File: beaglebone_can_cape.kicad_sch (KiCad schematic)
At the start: 26 parts, among them J1 Conn_01x02_Pin, J2 Conn_01x02_Pin, J3 DTM15-12PA, J4 Conn_02x02_Top_Bottom, J5 Battery Harness, P8 BeagleBone_Black_Header, P9 BeagleBone_Black_Header, U1 TCAN332, U2 TCAN332, U3 LMR51430

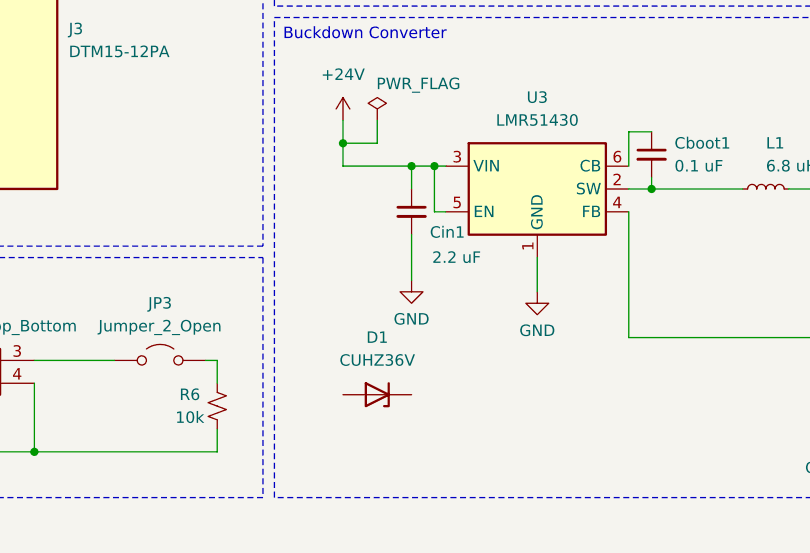
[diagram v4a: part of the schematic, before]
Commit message: added tvs diode to schem
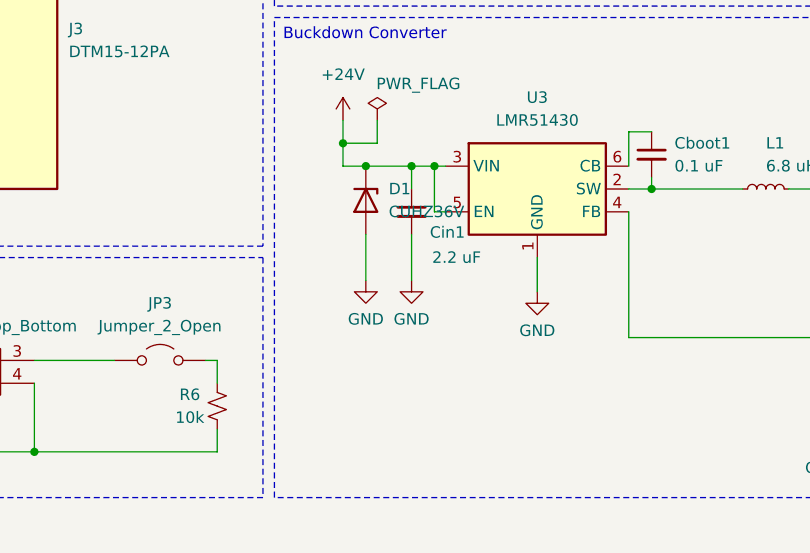
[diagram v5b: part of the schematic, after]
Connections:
- net +24V: now also D1.1 (K)
- net GND: now also D1.2 (A)
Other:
- moved on the sheet: D1
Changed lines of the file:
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@@
 	)
 	(junction
+		(at 96.52 139.7)
+		(diameter 0)
+		(color 0 0 0 0)
+	)
+	(junction
 		(at 104.14 139.7)
 		(diameter 0)
@@
 	(wire
 		(pts
+			(xy 96.52 147.32) (xy 96.52 152.4)
+		)
+		(stroke
+			(width 0)
+			(type default)
+		)
+	)
+	(wire
+		(pts
 			(xy 147.32 158.75) (xy 147.32 161.29)
 		)
@@
 	(wire
 		(pts
+			(xy 96.52 139.7) (xy 101.6 139.7)
+		)
+		(stroke
+			(width 0)
+			(type default)
+		)
+	)
+	(wire
+		(pts
 			(xy 138.43 46.99) (xy 140.97 46.99)
 		)
@@
 	(wire
 		(pts
-			(xy 93.98 139.7) (xy 101.6 139.7)
+			(xy 93.98 139.7) (xy 96.52 139.7)
 		)
 		(stroke
@@
 	(symbol
 		(lib_id "Diode:PTVS5V0Z1USK")
-		(at 97.79 165.1 180)
+		(at 96.52 143.51 270)
 		(unit 1)
 		(exclude_from_sim no)
@@
 		(fields_autoplaced yes)
 		(property "Reference" "D1"
-			(at 97.79 158.75 0)
+			(at 99.06 142.2399 90)
 			(effects
 				(font
 					(size 1.27 1.27)
 				)
+				(justify left)
 			)
 		)
 		(property "Value" "CUHZ36V"
-			(at 97.79 161.29 0)
+			(at 99.06 144.7799 90)
 			(effects
 				(font
 					(size 1.27 1.27)
 				)
+				(justify left)
 			)
 		)
 		(property "Footprint" "SeniorDesign:TVSDiode"
-			(at 97.79 160.655 0)
+			(at 92.075 143.51 0)
 			(effects
 				(font
@@
 		)
 		(property "Datasheet" "https://toshiba.semicon-storage.com/info/CUHZ36V_datasheet_en_20210917.pdf?did=70664&prodName=CUHZ36V"
-			(at 97.79 165.1 0)
+			(at 96.52 143.51 0)
 			(effects
 				(font
@@
 		)
 		(property "Description" ""
-			(at 97.79 165.1 0)
+			(at 96.52 143.51 0)
 			(effects
 				(font
@@
 					(unit 1)
 				)
+			)
+		)
+	)
+	(symbol
+		(lib_id "power:GND")
+		(at 96.52 152.4 0)
+		(unit 1)
+		(exclude_from_sim no)
+		(in_bom yes)
+		(on_board yes)
+		(dnp no)
+		(property "Reference" "#PWR022"
+			(at 96.52 158.75 0)
+			(effects
+				(font
+					(size 1.27 1.27)
+				)
+				(hide yes)
+			)
+		)
+		(property "Value" "GND"
+			(at 96.52 156.718 0)
+			(effects
+				(font
+					(size 1.27 1.27)
+				)
+			)
+		)
+		(property "Footprint" ""
+			(at 96.52 152.4 0)
+			(effects
+				(font
+					(size 1.27 1.27)
+				)
+				(hide yes)
+			)
+		)
+		(property "Datasheet" ""
+			(at 96.52 152.4 0)
+			(effects
+				(font
+					(size 1.27 1.27)
+				)
+				(hide yes)
+			)
+		)
+		(property "Description" "Power symbol creates a global label with name \"GND\" , ground"
+			(at 96.52 152.4 0)
+			(effects
+				(font
+					(size 1.27 1.27)
+				)
+				(hide yes)
+			)
+		)
+		(pin "1"
+		)
+		(instances
+			(project "beaglebone_can_cape"
+				(path "/e63e39d7-6ac0-4ffd-8aa3-1841a4541b55"
+					(reference "#PWR022")
+					(unit 1)
+				)

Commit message: pushing for nash work
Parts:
- J3: footprint Senior Design:TE_DTM15-12PA -> SeniorDesign:Deutsch_Marlin
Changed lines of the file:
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@@
 			)
 		)
-		(property "Footprint" "Senior Design:TE_DTM15-12PA"
+		(property "Footprint" "SeniorDesign:Deutsch_Marlin"
 			(at 57.15 127 0)
 			(effects

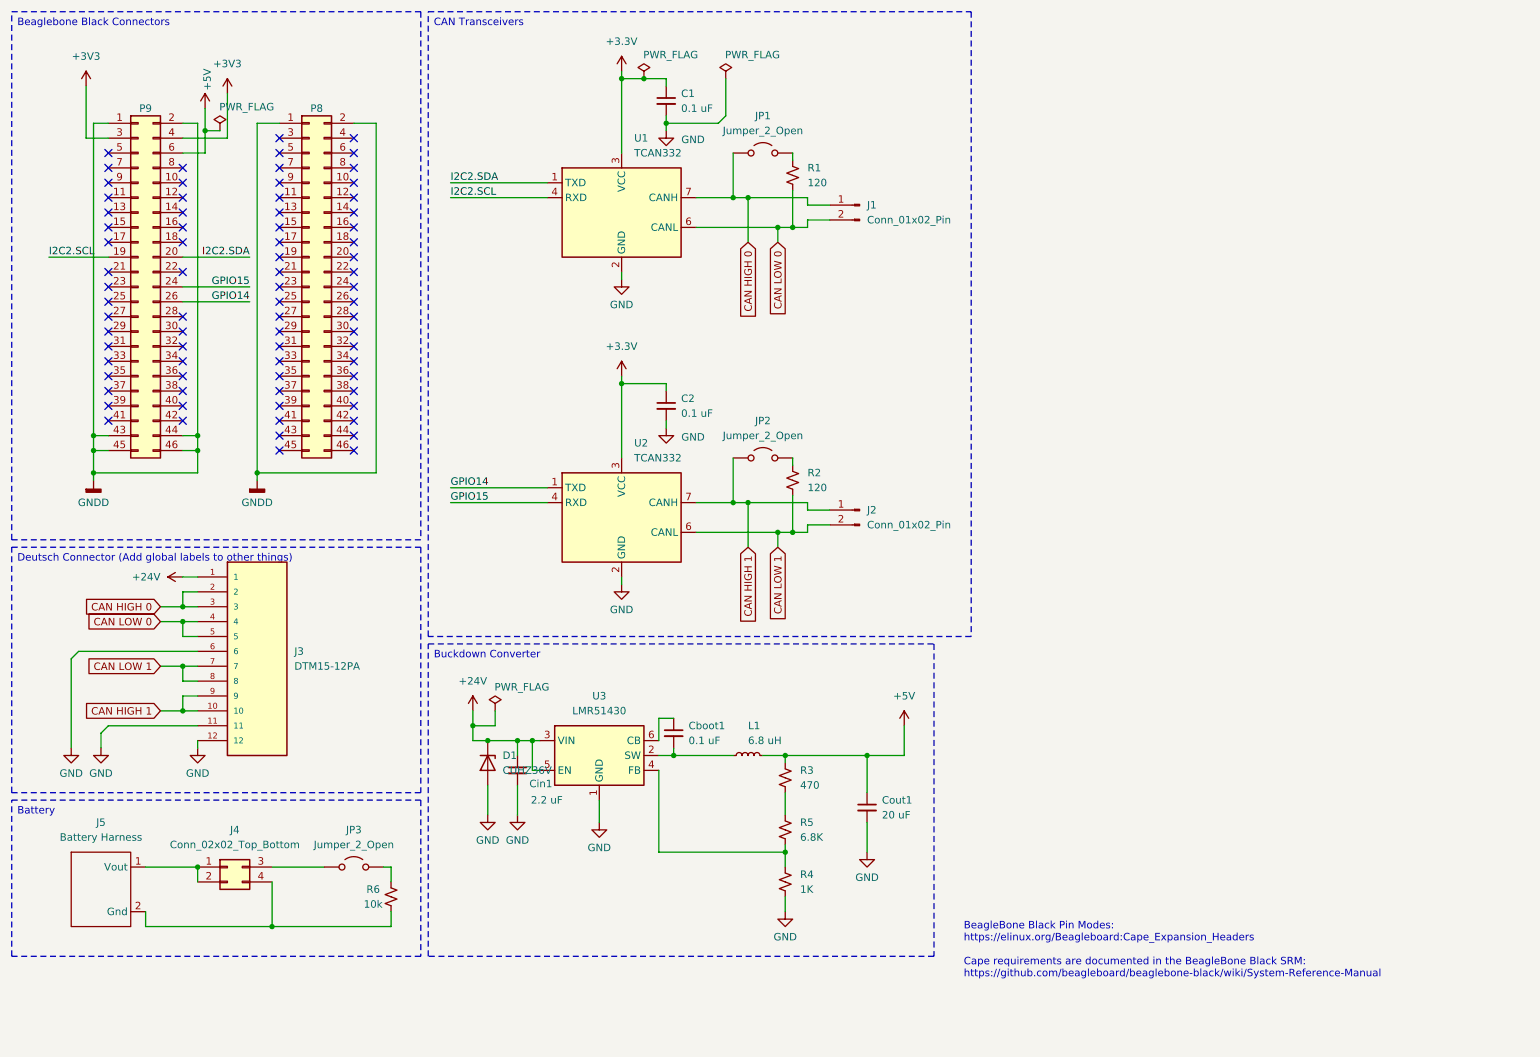
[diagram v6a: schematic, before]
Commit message: Implementing Deutsch + wiring
* Got rid of more errors and corrected more footprints. Going smoothly.
* Researched the TVS diode. cool stuff!
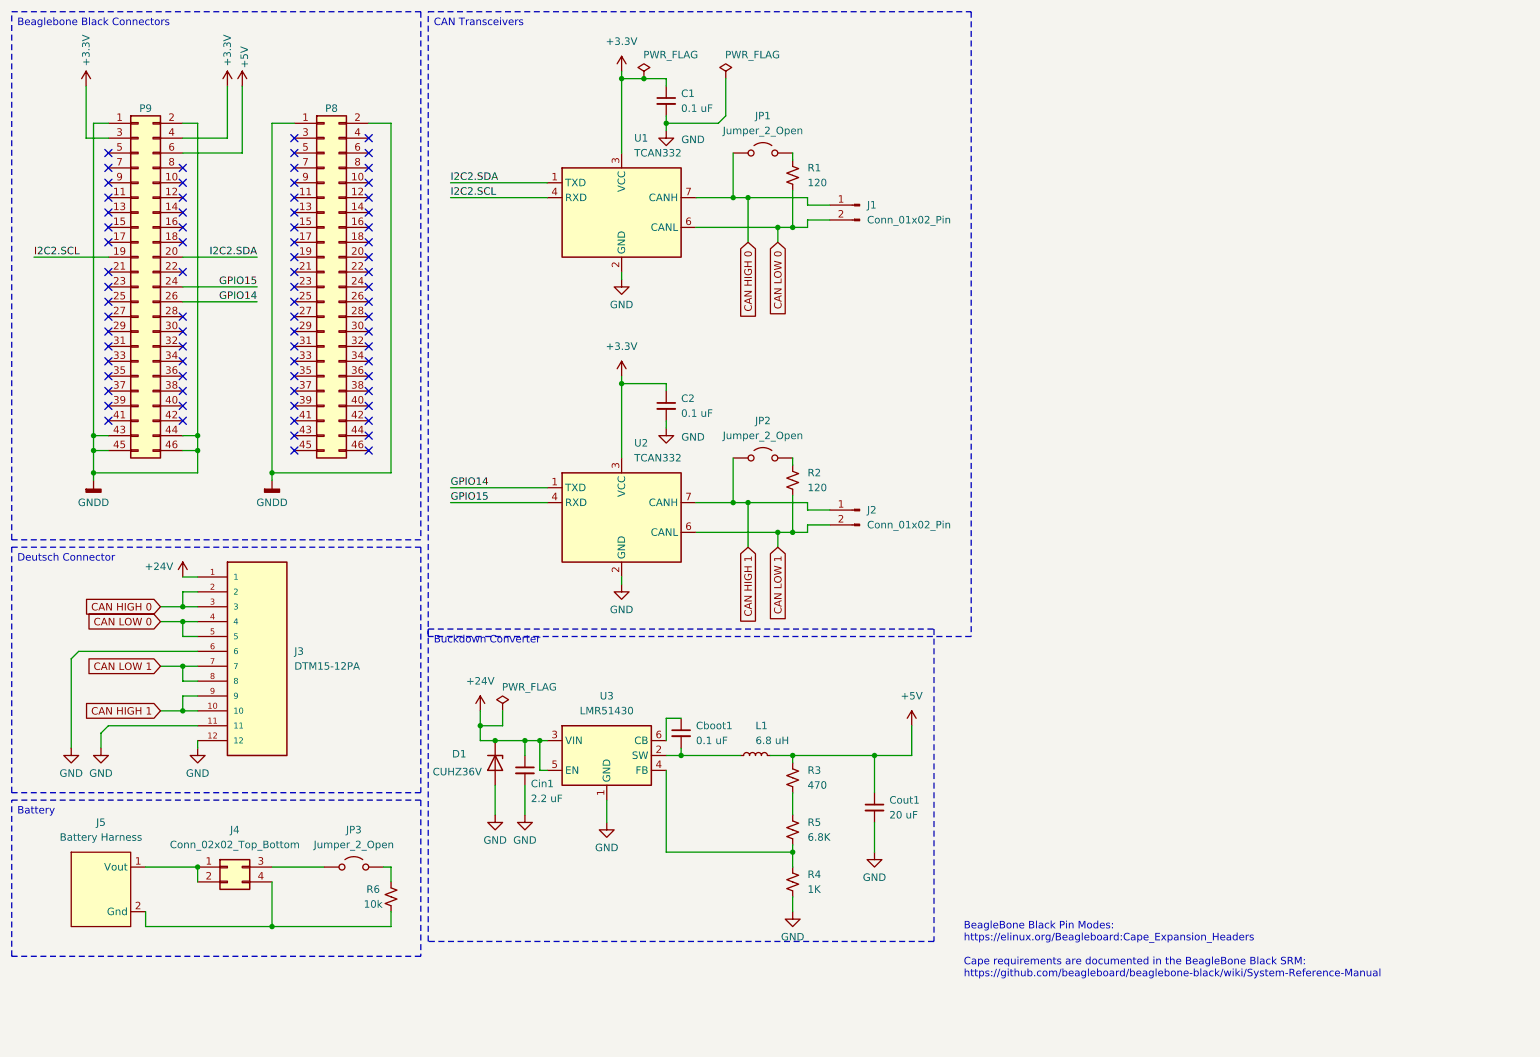
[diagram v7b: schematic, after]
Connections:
- net +3V3 is gone; now on net +3.3V: P9.3 (Pin_3), P9.4 (Pin_4)
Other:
- moved on the sheet: Cboot1, Cin1, Cout1, D1, L1, P8, R3, R4, R5, U3
